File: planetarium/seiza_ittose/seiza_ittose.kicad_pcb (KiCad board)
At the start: 2 copper layers, 94.5 x 66 mm, 29 parts, among them J1 Jack-DC, J10 Jack-DC, J11 Jack-DC, J12 Jack-DC, J13 Conn_01x03, J2 Jack-DC, J3 Jack-DC, J4 Jack-DC, J5 Jack-DC, J6 Jack-DC, J7 Jack-DC, J8 Jack-DC, J9 Jack-DC, Q1 TK25S06N1L, SW1 RotaryEncoder, SW2 RotaryEncoder, SW3 RotaryEncoder, SW4 RotaryEncoder, U1 XIAO-ESP32-C3-SMD, U2 TBD62783A

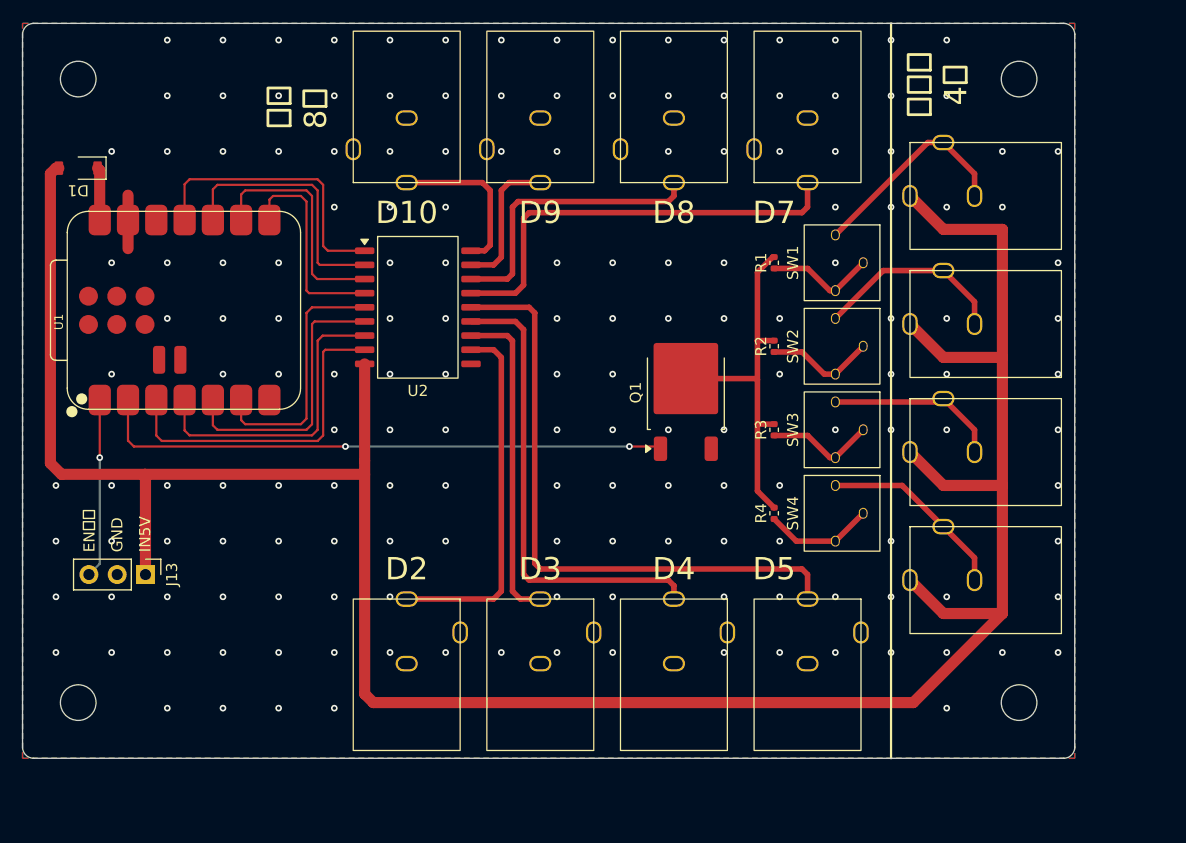
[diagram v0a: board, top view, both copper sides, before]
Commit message: change: LED追加, EN->nEN
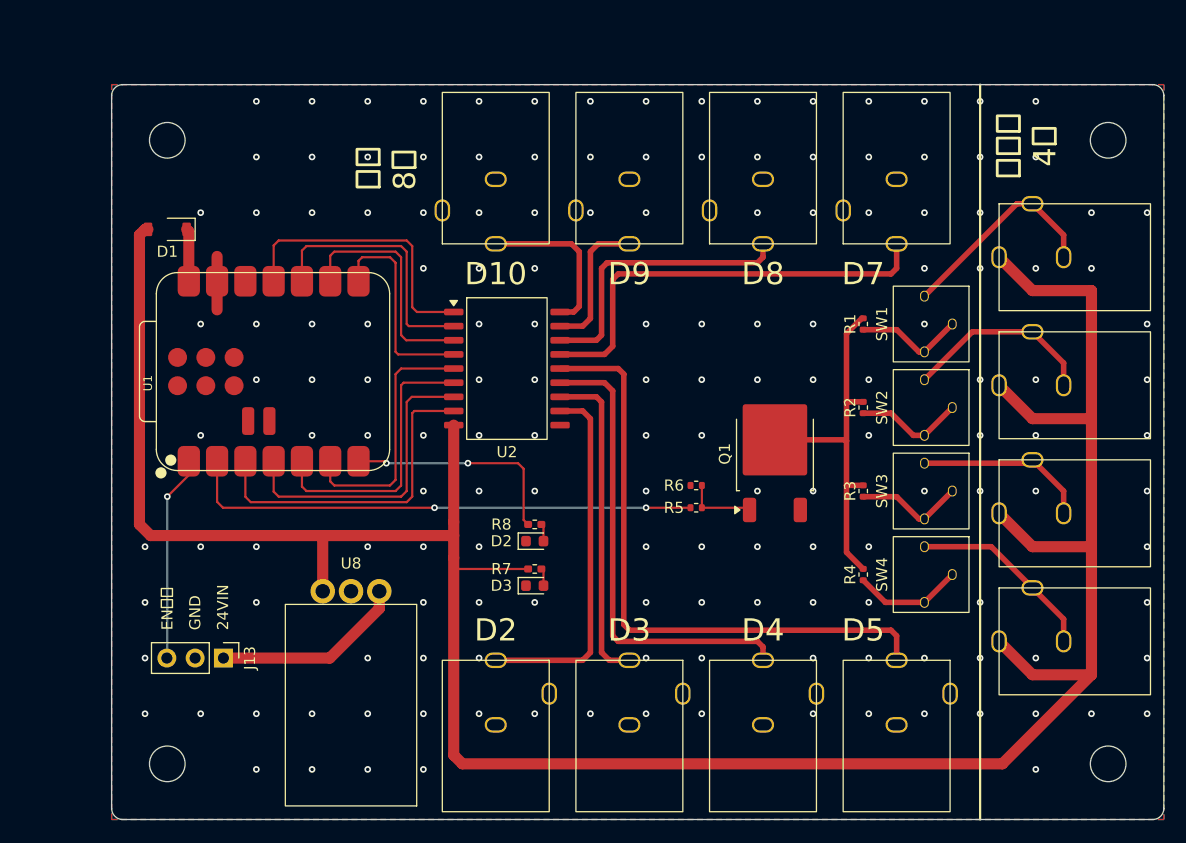
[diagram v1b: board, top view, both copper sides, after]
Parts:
- added D2: status, LED_SMD:LED_0603_1608Metric, F.Cu at (138.0, 105.0)
- added D3: pwr, LED_SMD:LED_0603_1608Metric, F.Cu at (138.0, 109.0)
- added R5: 100, Resistor_SMD:R_0402_1005Metric, F.Cu at (152.5, 102.0)
- added R6: 100k, Resistor_SMD:R_0402_1005Metric, F.Cu at (152.5, 100.0)
- added R7: 10k, Resistor_SMD:R_0402_1005Metric_Pad0.72x0.64mm_HandSolder, F.Cu at (138.0, 107.5)
- added R8: 10k, Resistor_SMD:R_0402_1005Metric_Pad0.72x0.64mm_HandSolder, F.Cu at (138.0, 103.5)
- added U8: R-78K5.0-2.0L, R-78K5.0-2.0L:R-78K5.0-2.0L, F.Cu at (121.5, 109.5)
- moved J13 10.3 mm to (110.0, 115.5)
- moved D1 9.71 mm to (105.0, 77.0)
- moved J1 9.71 mm to (170.5, 72.5)
- moved J10 9.71 mm to (185.5, 91.0)
- moved J11 9.71 mm to (185.5, 102.5)
- moved J12 9.71 mm to (185.5, 114.0)
- moved J2 9.71 mm to (158.5, 72.5)
- moved J3 9.71 mm to (146.5, 72.5)
- moved J4 9.71 mm to (134.5, 72.5)
- moved J5 9.71 mm to (170.5, 121.5)
- moved J6 9.71 mm to (158.5, 121.5)
- moved J7 9.71 mm to (146.5, 121.5)
- moved J8 9.71 mm to (134.5, 121.5)
- moved J9 9.71 mm to (185.5, 79.5)
- moved Q1 9.71 mm to (159.6, 97.2)
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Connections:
- J13 pad 1: +5V -> +24V
- Q1 pad 1: ITTOSE -> Net-(Q1-G)
- U1 pad 7: unconnected-(U1-PB08_A6_D6_TX-Pad7) -> /led_status
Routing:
- net /led_status: track 0.00 -> 20.3 mm, vias 0 -> 2
- net +24V: track 0.00 -> 17.4 mm
- net Net-(Q1-G): track 0.00 -> 6.37 mm
- net ITTOSE: track 51.8 -> 46.4 mm
- net +5V: track 227.9 -> 230.5 mm
- net kousei_en: track 16.1 -> 18.5 mm
- net Net-(D3-A): track 0.00 -> 1.58 mm
- net Net-(D2-A): track 0.00 -> 1.58 mm
- net GND: vias 168 -> 159
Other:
- board text added: "24VIN"
- board text removed: "IN5V"
